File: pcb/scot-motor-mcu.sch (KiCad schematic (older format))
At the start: 13 parts

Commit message: WIP.
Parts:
- added C? (x2): C, symbol Device:C
- added C? (x4): 100n, symbol Device:C
- added D? (x4): LED, symbol Device:LED
- added FB?: Ferrite_Bead_Small, symbol Device:Ferrite_Bead_Small
- added IC?: STM32F0xxKxTx, agg:LQFP-32, symbol agg-kicad:STM32F0xxKxTx
- added J?: Conn_01x03_Male, symbol Connector:Conn_01x03_Male
- added P?: SWD, agg:FTSH-105-01-F-D-K, symbol agg-kicad:SWD
- added R?: 1K, symbol Device:R
- added R? (x4): R, symbol Device:R
- added R? (x6): 47R, symbol Device:R
- added R? (x3): 4K7, symbol Device:R
- added U? (x3): LTV-357T, Package_SO:SO-4_4.4x3.6mm_P2.54mm, symbol Isolator:LTV-357T
- added Y?: Crystal_GND24, symbol Device:Crystal_GND24
- C?: value 10u -> 100n
- R? (x2): value R -> 330R
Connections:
- net labels added: 3V3_MCU, CAN_MCU_RX, CAN_MCU_TX, CONTROL_OK, ESTOP_3V3, ESTOP_A, ESTOP_B, LIMIT_1, LIMIT_1_INPUT, LIMIT_2, LIMIT_2_INPUT, LV_GND, MOTOR_VCC, PWM_CH1, PWM_CH2, SWD_CLK, SWD_IO, UART_DEBUG_RX, UART_DEBUG_TX, VI_ALERT, VI_I2C_SCL, VI_I2C_SDA, nFAULT
- wire segments 53 -> 178
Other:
- note added: "74AC00: Max 12mA output, so set LED for 10mA max."
- note added: "CONTROL_OK (BLUE)"
- note added: "FAULT (RED)"
- note added: "I2C_VI: I2C1"
- note added: "LIMIT_1 (RED)"
- note added: "LIMIT_2 (RED)"
- note added: "PWM_1: TIM1_CH1"
- note added: "PWM_2: TIM1_CH2"
- note added: "SOIC-14 package (74AC00D)"
- note added: "SOP-4 Package"
- note added: "UART Port for debugging"
- note added: "UART_DEBUG: USART2"
- note added: "VCC = 28V IN"
- moved on the sheet: C?, R?, U?C, U?D, U?E

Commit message: WIP.
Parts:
- added C14: 100n/50V, Capacitor_SMD:C_0603_1608Metric_Pad1.05x0.95mm_HandSolder, symbol Device:C
- C10, C4, C5, C8, C9: renamed from C?; value 100n -> 100n/3V3; footprint (none) -> Capacitor_SMD:C_0603_1608Metric_Pad1.05x0.95mm_HandSolder
- C11: renamed from C?; value 100n -> 100n/50V; footprint (none) -> Capacitor_SMD:C_0603_1608Metric_Pad1.05x0.95mm_HandSolder
- C12: renamed from C?; value 10u -> 10u/50V; footprint (none) -> Capacitor_SMD:C_1210_3225Metric_Pad1.42x2.65mm_HandSolder
- C13, C15: renamed from C?; value 22u/35V -> 22u/50V; footprint (none) -> Capacitor_SMD:CP_Elec_8x10.5
- C6, C7: renamed from C?; value C -> 12p; footprint (none) -> Capacitor_SMD:C_0603_1608Metric_Pad1.05x0.95mm_HandSolder
- D1, D2, D3, D4: renamed from D?; footprint (none) -> LED_SMD:LED_1210_3225Metric_Pad1.42x2.65mm_HandSolder
- FB1: renamed from FB?; footprint (none) -> Inductor_SMD:L_0805_2012Metric_Pad1.15x1.40mm_HandSolder
- J8: renamed from J?; footprint (none) -> Connector_PinHeader_2.54mm:PinHeader_1x03_P2.54mm_Vertical
- R10, R11, R8: renamed from R?; value R -> 62R; footprint (none) -> Resistor_SMD:R_0805_2012Metric_Pad1.15x1.40mm_HandSolder
- R12, R13, R14, R15, R6, R7: renamed from R?; footprint (none) -> Resistor_SMD:R_0805_2012Metric_Pad1.15x1.40mm_HandSolder
- R16, R17, R2, R3, R5, R9: renamed from R?; footprint (none) -> Resistor_SMD:R_0603_1608Metric_Pad1.05x0.95mm_HandSolder
- R4: renamed from R?; value R -> 18R; footprint (none) -> Resistor_SMD:R_0805_2012Metric_Pad1.15x1.40mm_HandSolder
- U2: renamed from U?; footprint (none) -> agg:SOIC-14
- Y1: renamed from Y?; footprint (none) -> Crystal:Crystal_SMD_Abracon_ABM8G-4Pin_3.2x2.5mm
- gave numbers to parts that had none: 6
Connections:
- net labels removed: LV_GND
- wire segments 178 -> 184

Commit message: pcb: Add brake clutch driver.
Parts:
- added D6: SS16HE, agg:SOD-323, symbol Device:D_Schottky
- added IC3: NCV8450A, Package_TO_SOT_SMD:SOT-223-3_TabPin2, symbol agg-kicad:NCV8450A
- added Q1: BC817, Package_TO_SOT_SMD:SOT-23, symbol Transistor_BJT:BC817
- added R20: 4K7, Resistor_SMD:R_0603_1608Metric_Pad1.05x0.95mm_HandSolder, symbol Device:R
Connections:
- net labels added: POWER_28V+, nBRAKE, nBRAKE_DRIVE
- wire segments 184 -> 194
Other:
- note added: "0.4mA"
- note added: "200mA expected"
- moved on the sheet: C10, C13, C15, U2E
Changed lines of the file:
@@
 $Descr A4 11693 8268
 encoding utf-8
-Sheet 3 4
+Sheet 4 4
 Title ""
 Date ""
@@
 L 74xx:74HC00 U2
 U 5 1 5E56678C
-P 8700 2100
-F 0 "U2" H 8930 2146 50  0000 L CNN
-F 1 "74HC00" H 8930 2055 50  0000 L CNN
-F 2 "agg:SOIC-14" H 8700 2100 50  0001 C CNN
-F 3 "http://www.ti.com/lit/gpn/sn74hc00" H 8700 2100 50  0001 C CNN
-	5    8700 2100
+P 8600 5800
+F 0 "U2" H 8830 5846 50  0000 L CNN
+F 1 "74HC00" H 8830 5755 50  0000 L CNN
+F 2 "agg:SOIC-14" H 8600 5800 50  0001 C CNN
+F 3 "http://www.ti.com/lit/gpn/sn74hc00" H 8600 5800 50  0001 C CNN
+	5    8600 5800
 	1    0    0    -1
 $EndComp
@@
 L agg-kicad:3v3 #PWR0104
 U 1 1 5E61B627
-P 8700 1550
-F 0 "#PWR0104" H 8700 1660 50  0001 L CNN
-F 1 "3v3" H 8700 1673 50  0000 C CNN
-F 2 "" H 8700 1550 50  0001 C CNN
-F 3 "" H 8700 1550 50  0001 C CNN
-	1    8700 1550
-	1    0    0    -1
-$EndComp
-Wire Wire Line
-	8700 1600 8700 1550
+P 8600 5250
+F 0 "#PWR0104" H 8600 5360 50  0001 L CNN
+F 1 "3v3" H 8600 5373 50  0000 C CNN
+F 2 "" H 8600 5250 50  0001 C CNN
+F 3 "" H 8600 5250 50  0001 C CNN
+	1    8600 5250
+	1    0    0    -1
+$EndComp
+Wire Wire Line
+	8600 5300 8600 5250
 $Comp
 L Device:C C10
 U 1 1 5E61E517
-P 9350 2050
-F 0 "C10" H 9465 2096 50  0000 L CNN
-F 1 "100n/3V3" H 9465 2005 50  0000 L CNN
-F 2 "Capacitor_SMD:C_0603_1608Metric_Pad1.05x0.95mm_HandSolder" H 9388 1900 50  0001 C CNN
-F 3 "~" H 9350 2050 50  0001 C CNN
-	1    9350 2050
-	1    0    0    -1
-$EndComp
-Wire Wire Line
-	9350 2200 9350 2600
-Wire Wire Line
-	9350 2600 9050 2600
-Wire Wire Line
-	9350 1900 9350 1600
-Wire Wire Line
-	9350 1600 8700 1600
-Connection ~ 8700 1600
+P 9250 5750
+F 0 "C10" H 9365 5796 50  0000 L CNN
+F 1 "100n/3V3" H 9365 5705 50  0000 L CNN
+F 2 "Capacitor_SMD:C_0603_1608Metric_Pad1.05x0.95mm_HandSolder" H 9288 5600 50  0001 C CNN
+F 3 "~" H 9250 5750 50  0001 C CNN
+	1    9250 5750
+	1    0    0    -1
+$EndComp
+Wire Wire Line
+	9250 5900 9250 6300
+Wire Wire Line
+	9250 6300 8950 6300
+Wire Wire Line
+	9250 5600 9250 5300
+Wire Wire Line
+	9250 5300 8600 5300
+Connection ~ 8600 5300
 $Comp
 L agg-kicad:VCC #PWR0105
@@
 L agg-kicad:VCC #PWR0106
 U 1 1 5E6A00FE
-P 10150 1850
-F 0 "#PWR0106" H 10150 1960 50  0001 L CNN
-F 1 "VCC" H 10150 1973 50  0000 C CNN
-F 2 "" H 10150 1850 50  0001 C CNN
-F 3 "" H 10150 1850 50  0001 C CNN
-	1    10150 1850
+P 10200 5500
+F 0 "#PWR0106" H 10200 5610 50  0001 L CNN
+F 1 "VCC" H 10200 5623 50  0000 C CNN
+F 2 "" H 10200 5500 50  0001 C CNN
+F 3 "" H 10200 5500 50  0001 C CNN
+	1    10200 5500
 	1    0    0    -1
 $EndComp
@@
 L Device:CP C13
 U 1 1 5E6A417D
-P 9950 2050
-F 0 "C13" H 10068 2096 50  0000 L CNN
-F 1 "22u/50V" H 10068 2005 50  0000 L CNN
-F 2 "Capacitor_SMD:CP_Elec_8x10.5" H 9988 1900 50  0001 C CNN
-F 3 "~" H 9950 2050 50  0001 C CNN
-	1    9950 2050
+P 10000 5700
+F 0 "C13" H 10118 5746 50  0000 L CNN
+F 1 "22u/50V" H 10118 5655 50  0000 L CNN
+F 2 "Capacitor_SMD:CP_Elec_8x10.5" H 10038 5550 50  0001 C CNN
+F 3 "~" H 10000 5700 50  0001 C CNN
+	1    10000 5700
 	1    0    0    -1
 $EndComp
@@
 L Device:CP C15
 U 1 1 5E6A4BEF
-P 10550 2050
-F 0 "C15" H 10668 2096 50  0000 L CNN
-F 1 "22u/50V" H 10668 2005 50  0000 L CNN
-F 2 "Capacitor_SMD:CP_Elec_8x10.5" H 10588 1900 50  0001 C CNN
-F 3 "~" H 10550 2050 50  0001 C CNN
-	1    10550 2050
+P 10600 5700
+F 0 "C15" H 10718 5746 50  0000 L CNN
+F 1 "22u/50V" H 10718 5655 50  0000 L CNN
+F 2 "Capacitor_SMD:CP_Elec_8x10.5" H 10638 5550 50  0001 C CNN
+F 3 "~" H 10600 5700 50  0001 C CNN
+	1    10600 5700
 	1    0    0    -1
 $EndComp
 Text Notes 7750 4850 0    50   ~ 10
 NAND Gate, actually use 74AC00?? (check availability)
-Text Notes 9950 1650 0    50   ~ 0
+Text Notes 10000 5300 0    50   ~ 0
 VCC = 28V IN
 $Comp
@@
 UART Port for debugging
 Wire Wire Line
-	10550 2250 10550 2200
-Wire Wire Line
-	9950 2250 9950 2200
-Wire Wire Line
-	9950 1900 9950 1850
-Wire Wire Line
-	9950 1850 10150 1850
-Wire Wire Line
-	10550 1900 10550 1850
-Wire Wire Line
-	10550 1850 10150 1850
-Connection ~ 10150 1850
+	10600 5900 10600 5850
+Wire Wire Line
+	10000 5900 10000 5850
+Wire Wire Line
+	10000 5550 10000 5500
+Wire Wire Line
+	10000 5500 10200 5500
+Wire Wire Line
+	10600 5550 10600 5500
+Wire Wire Line
+	10600 5500 10200 5500
+Connection ~ 10200 5500
 Wire Wire Line
 	6300 4800 4650 4800
@@
 $EndComp
 Wire Wire Line
-	9950 2250 10250 2250
+	10000 5900 10300 5900
 $Comp
 L power:GND #PWR0115
@@
 L power:GND #PWR0117
 U 1 1 5EB441CE
-P 10250 2250
-F 0 "#PWR0117" H 10250 2000 50  0001 C CNN
-F 1 "GND" H 10255 2077 50  0000 C CNN
-F 2 "" H 10250 2250 50  0001 C CNN
-F 3 "" H 10250 2250 50  0001 C CNN
-	1    10250 2250
-	1    0    0    -1
-$EndComp
-Connection ~ 10250 2250
-Wire Wire Line
-	10250 2250 10550 2250
+P 10300 5900
+F 0 "#PWR0117" H 10300 5650 50  0001 C CNN
+F 1 "GND" H 10305 5727 50  0000 C CNN
+F 2 "" H 10300 5900 50  0001 C CNN
+F 3 "" H 10300 5900 50  0001 C CNN
+	1    10300 5900
+	1    0    0    -1
+$EndComp
+Connection ~ 10300 5900
+Wire Wire Line
+	10300 5900 10600 5900
 Wire Wire Line
 	4150 3800 4700 3800
@@
 L power:GND #PWR0125
 U 1 1 5E8C0346
-P 9050 2600
-F 0 "#PWR0125" H 9050 2350 50  0001 C CNN
-F 1 "GND" H 9055 2427 50  0000 C CNN
-F 2 "" H 9050 2600 50  0001 C CNN
-F 3 "" H 9050 2600 50  0001 C CNN
-	1    9050 2600
-	1    0    0    -1
-$EndComp
-Connection ~ 9050 2600
-Wire Wire Line
-	9050 2600 8700 2600
+P 8950 6300
+F 0 "#PWR0125" H 8950 6050 50  0001 C CNN
+F 1 "GND" H 8955 6127 50  0000 C CNN
+F 2 "" H 8950 6300 50  0001 C CNN
+F 3 "" H 8950 6300 50  0001 C CNN
+	1    8950 6300
+	1    0    0    -1
+$EndComp
+Connection ~ 8950 6300
+Wire Wire Line
+	8950 6300 8600 6300
 $Comp
 L power:GND #PWR0126
@@
 Wire Wire Line
 	10250 3900 10550 3900
+$Comp
+L agg-kicad:NCV8450A IC3
+U 1 1 5E8EEAEF
+P 9450 1550
+F 0 "IC3" H 9450 1875 50  0000 C CNN
+F 1 "NCV8450A" H 9450 1784 50  0000 C CNN
+F 2 "Package_TO_SOT_SMD:SOT-223-3_TabPin2" H 9250 1250 50  0001 L CNN
+F 3 "https://www.onsemi.com/pub/Collateral/NCV8450-D.PDF" H 9250 1150 50  0001 L CNN
+F 4 "863-NCV8450ASTT3G" H 9250 1050 50  0001 L CNN "Mouser"
+	1    9450 1550
+	1    0    0    -1
+$EndComp
+Text HLabel 8900 1450 0    50   Input ~ 0
+POWER_28V+
+Wire Wire Line
+	9150 1450 8900 1450
+Text HLabel 10250 1450 2    50   Input ~ 0
+nBRAKE_DRIVE
+Wire Wire Line
+	10250 1450 9950 1450
+$Comp
+L Transistor_BJT:BC817 Q1
+U 1 1 5EA12C7C
+P 9050 1900
+F 0 "Q1" H 9241 1946 50  0000 L CNN
+F 1 "BC817" H 9241 1855 50  0000 L CNN
+F 2 "Package_TO_SOT_SMD:SOT-23" H 9250 1825 50  0001 L CIN
+F 3 "http://www.fairchildsemi.com/ds/BC/BC817.pdf" H 9050 1900 50  0001 L CNN
+	1    9050 1900
+	1    0    0    -1
+$EndComp
+$Comp
+L power:GND #PWR0139
+U 1 1 5EA14A70
+P 9150 2100
+F 0 "#PWR0139" H 9150 1850 50  0001 C CNN
+F 1 "GND" H 9155 1927 50  0000 C CNN
+F 2 "" H 9150 2100 50  0001 C CNN
+F 3 "" H 9150 2100 50  0001 C CNN
+	1    9150 2100
+	1    0    0    -1
+$EndComp
+Wire Wire Line
+	9150 1550 9150 1700
+$Comp
+L Device:R R20
+U 1 1 5EA40B75
+P 8700 1900
+F 0 "R20" V 8493 1900 50  0000 C CNN
+F 1 "4K7" V 8584 1900 50  0000 C CNN
+F 2 "Resistor_SMD:R_0603_1608Metric_Pad1.05x0.95mm_HandSolder" V 8630 1900 50  0001 C CNN
+F 3 "~" H 8700 1900 50  0001 C CNN
+	1    8700 1900
+	0    1    1    0
+$EndComp
+Text Notes 8600 2050 0    50   ~ 0
+0.4mA
+Wire Wire Line
+	4150 2700 4700 2700
+Wire Wire Line
+	3350 4200 2500 4200
+Text Label 2500 4200 0    50   ~ 0
+nBRAKE
+Text Label 8250 1900 0    50   ~ 0
+nBRAKE
+Wire Wire Line
+	8550 1900 8250 1900
+Text Notes 9800 1350 0    50   ~ 0
+200mA expected
+$Comp
+L Device:D_Schottky D6
+U 1 1 5EAD47CA
+P 9950 1650
+F 0 "D6" V 9904 1729 50  0000 L CNN
+F 1 "SS16HE" V 9995 1729 50  0000 L CNN
+F 2 "agg:SOD-323" H 9950 1650 50  0001 C CNN
+F 3 "~" H 9950 1650 50  0001 C CNN
+	1    9950 1650
+	0    1    1    0
+$EndComp
+Wire Wire Line
+	9950 1500 9950 1450
+Connection ~ 9950 1450
+Wire Wire Line
+	9950 1450 9750 1450
+Wire Wire Line
+	9950 1800 9950 2100
+Wire Wire Line
+	9950 2100 9150 2100
+Connection ~ 9150 2100
 $EndSCHEMATC

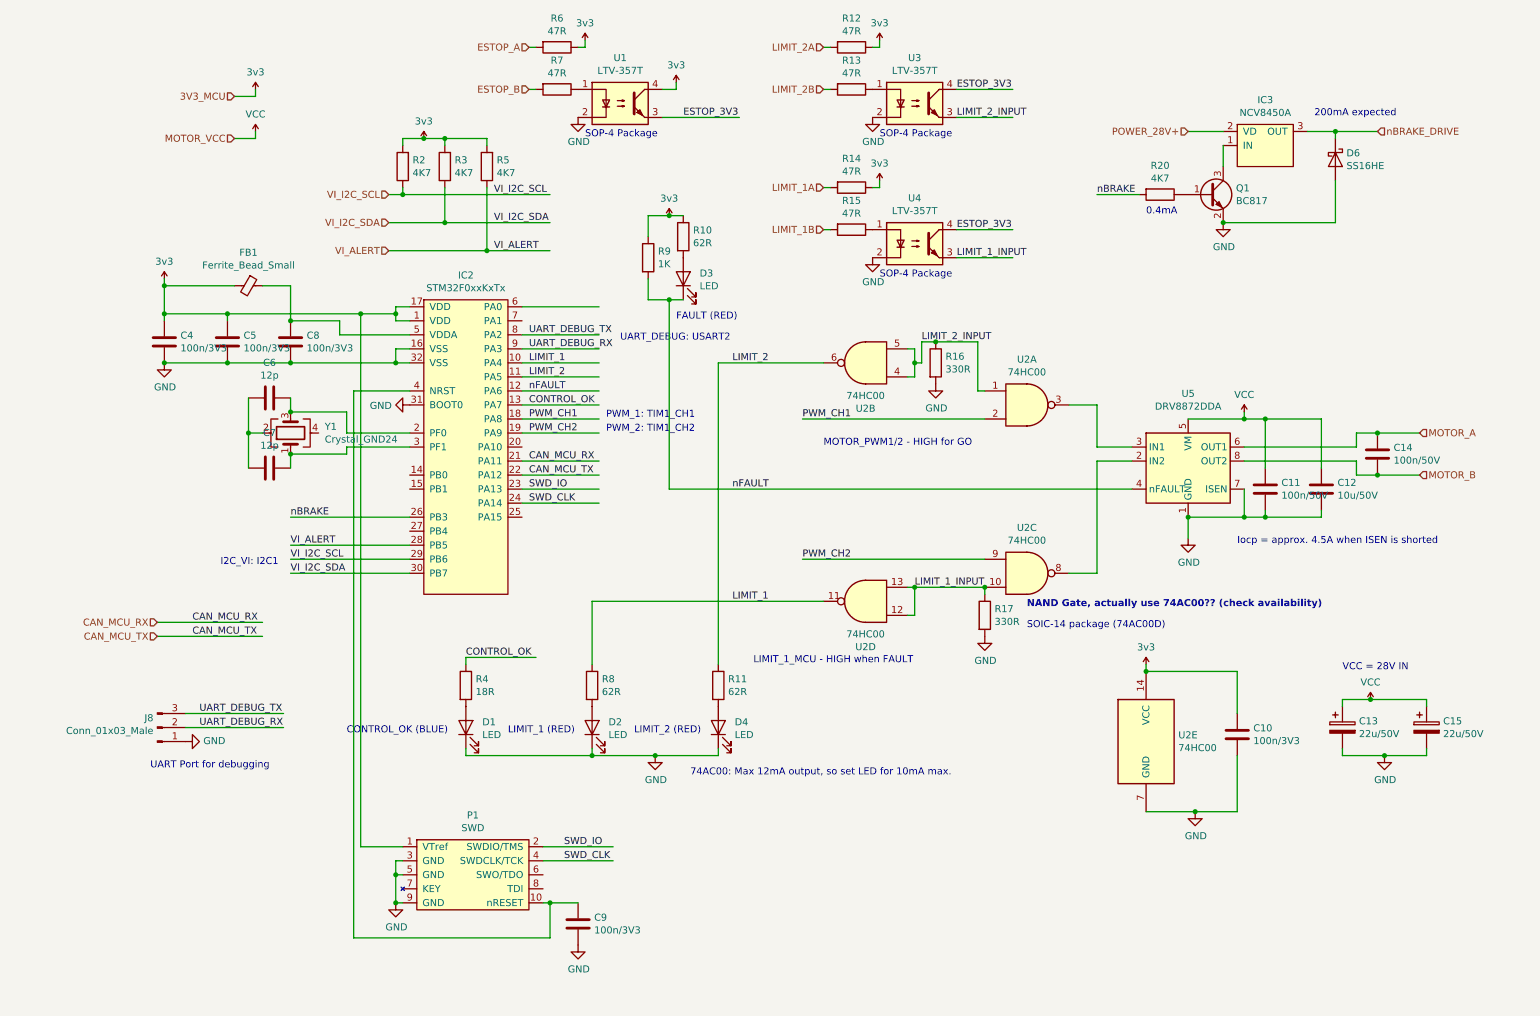
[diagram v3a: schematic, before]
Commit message: pcb: Link brake clutch to e-stop, aesthetic tweaks.
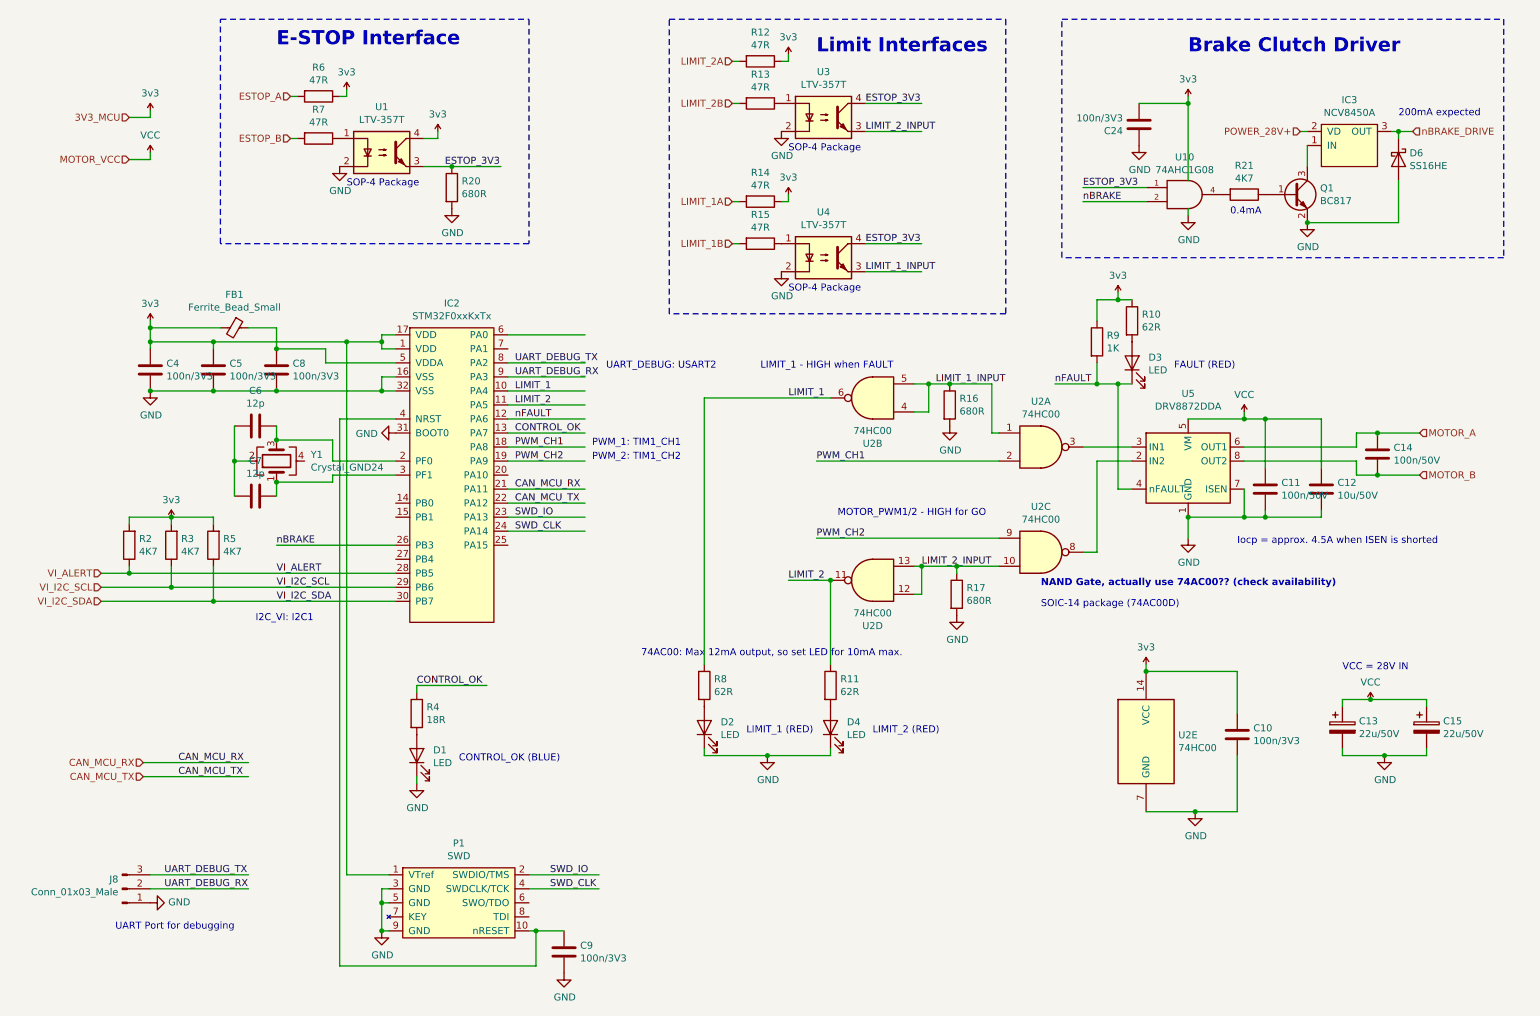
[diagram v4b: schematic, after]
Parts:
- added C24: 100n/3V3, Capacitor_SMD:C_0603_1608Metric_Pad1.05x0.95mm_HandSolder, symbol Device:C
- added R21: 4K7, Resistor_SMD:R_0603_1608Metric_Pad1.05x0.95mm_HandSolder, symbol Device:R
- added U10: 74AHC1G08, agg:SOT-23-5, symbol 74xGxx:74AHC1G08
- R16, R17: value 330R -> 680R
- R20: value 4K7 -> 680R
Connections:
- wire segments 194 -> 193
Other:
- note added: "Brake Clutch Driver"
- note added: "E-STOP Interface"
- note added: "LIMIT_1 - HIGH when FAULT"
- note added: "Limit Interfaces"
- note removed: "LIMIT_1_MCU - HIGH when FAULT"
- moved on the sheet: C4, C5, C6, C7, C8, C9, D1, D2, D3, D4, D6, FB1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
